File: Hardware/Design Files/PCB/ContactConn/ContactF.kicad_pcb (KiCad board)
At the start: 2 copper layers, 56.9 x 55 mm, 9 parts, among them P1 CONN_01X01, P2 CONN_01X01, P3 CONN_01X01, P4 CONN_01X01, P5 CONN_01X01, P6 CONN_01X01, P7 CONN_01X01, P8 CONN_01X01, P9 CONN_01X01

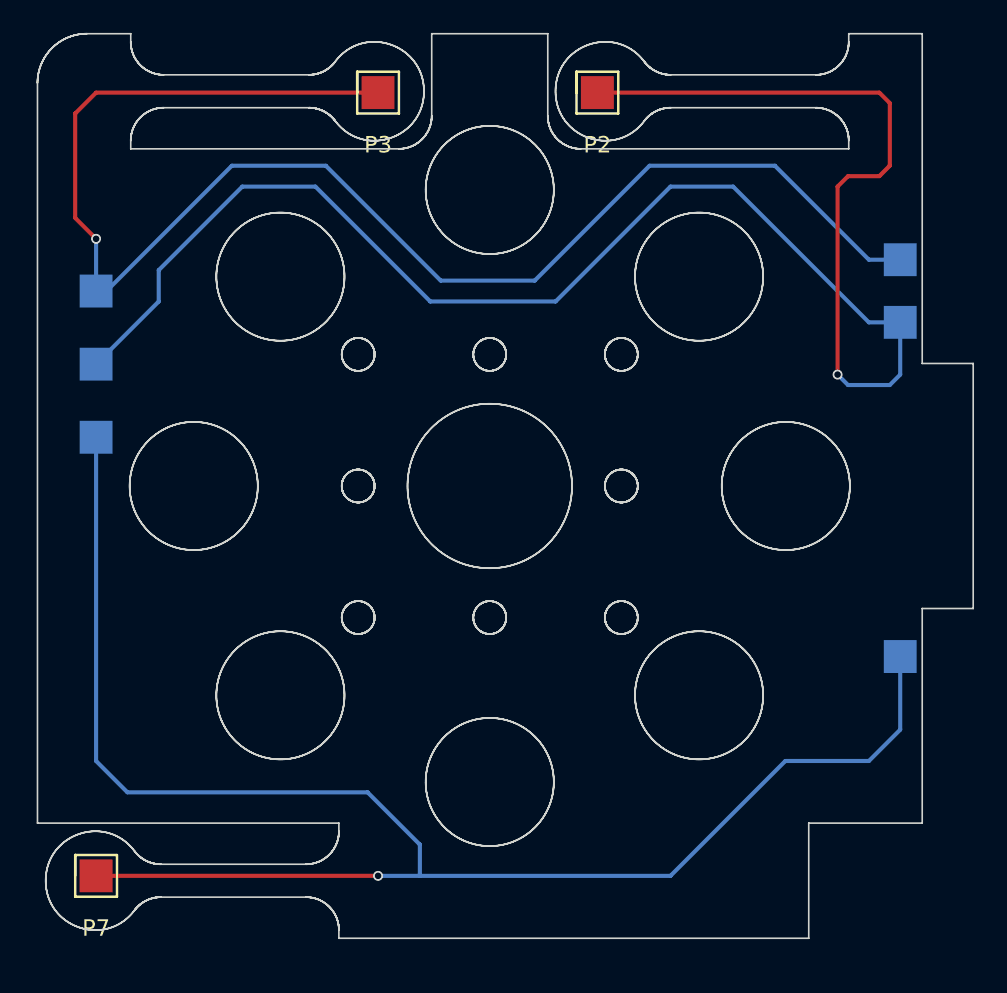
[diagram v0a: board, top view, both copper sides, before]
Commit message: Updated PCB and CAD files to reflect changes in the module connectors
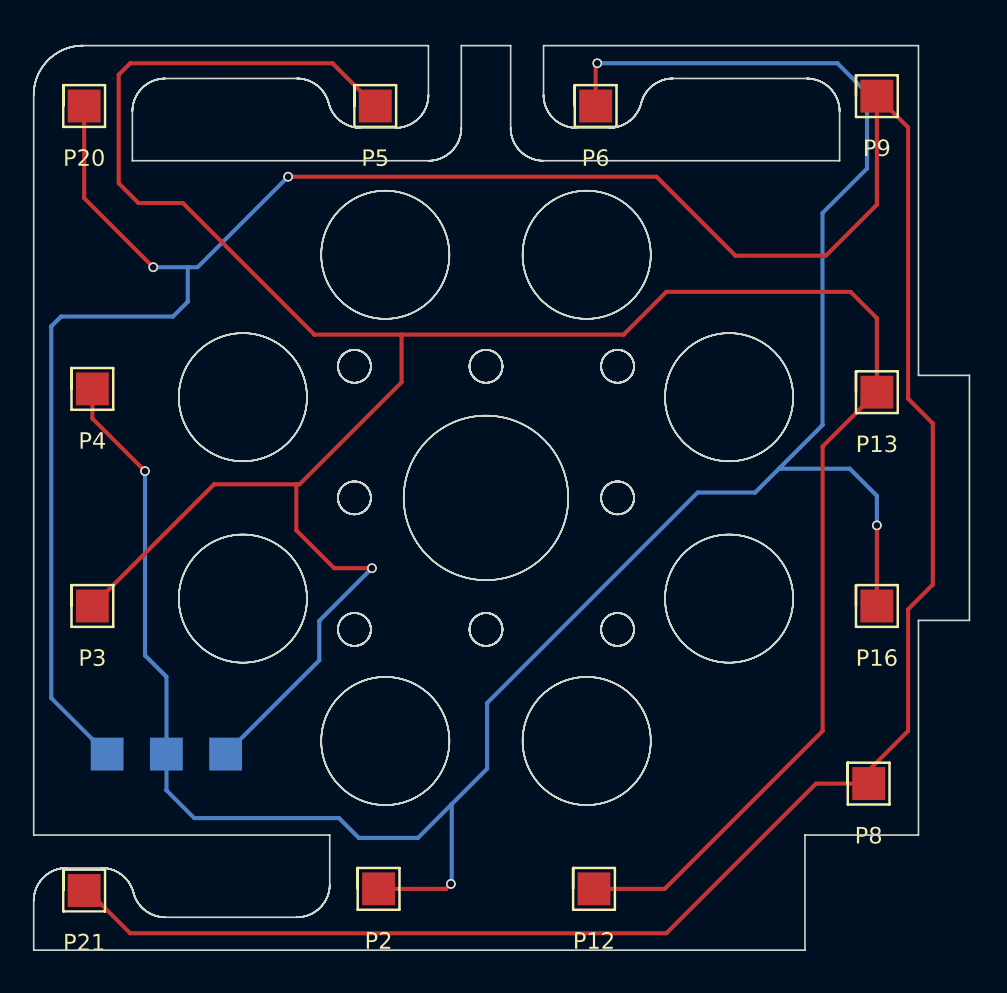
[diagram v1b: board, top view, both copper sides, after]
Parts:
- added P12: CONN_01X01, myfootprint:MYCONN2, F.Cu at (154.1, 118.9)
- added P13: CONN_01X01, myfootprint:MYCONN2, F.Cu at (171.3, 88.7)
- added P16: CONN_01X01, myfootprint:MYCONN2, F.Cu at (171.3, 101.7)
- added P17: CONN_01X01, myfootprint:MYCONN2, B.Cu at (128.1, 110.7)
- added P20: CONN_01X01, myfootprint:MYCONN2, F.Cu at (123.1, 71.3)
- added P21: CONN_01X01, myfootprint:MYCONN2, F.Cu at (123.1, 119.0)
- P4, P5, P6, P8, P9: moved to F.Cu
- P7: moved to B.Cu
- moved P8 51.5 mm to (170.8, 112.5)
- moved P1 50.9 mm to (131.7, 110.7)
- moved P2 50.2 mm to (141.0, 118.9)
- moved P3 35.7 mm to (123.6, 101.7)
- moved P9 34.1 mm to (171.3, 70.7)
- moved P6 22.7 mm to (154.2, 71.3)
- moved P5 20.4 mm to (140.8, 71.3)
- moved P7 7.44 mm to (124.5, 110.7)
- moved P4 1.52 mm to (123.6, 88.5)
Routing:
- net Net-(P20-Pad1): track 100.4 -> 203.5 mm, vias 1 -> 2
- net VCC: track 90.5 -> 170.2 mm
- net GND: track 108.2 -> 143.9 mm, vias 1 -> 4
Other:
- outline, holes or cut-outs redrawn
